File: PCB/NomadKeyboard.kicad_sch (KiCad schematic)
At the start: 94 parts, among them J1 4PIN, J2 OLED, P1 i2c_pin, P2 i2c_pin, SW1 SW_PUSH_LED, SW10 SW_PUSH_LED, SW11 SW_PUSH_LED, SW12 SW_PUSH_LED, SW13 SW_PUSH_LED, SW14 SW_PUSH_LED, SW15 SW_PUSH_LED, SW16 SW_PUSH_LED, SW17 SW_PUSH_LED, SW18 SW_PUSH_LED, SW19 SW_PUSH_LED, SW2 SW_PUSH_LED, SW20 SW_PUSH_LED, SW21 SW_PUSH_LED, SW22 SW_PUSH_LED, SW23 SW_PUSH_LED, SW24 SW_PUSH_LED, SW25 SW_PUSH_LED, SW26 SW_PUSH_LED, SW27 SW_PUSH_LED, SW28 SW_PUSH_LED, SW29 SW_PUSH_LED, SW3 SW_PUSH_LED, SW30 SW_PUSH_LED, SW31 SW_PUSH_LED, SW32 SW_PUSH_LED, SW33 SW_PUSH_LED, SW34 SW_PUSH_LED, SW4 SW_PUSH_LED, SW5 SW_PUSH_LED, SW6 SW_PUSH_LED, SW7 SW_PUSH_LED, SW8 SW_PUSH_LED, SW9 SW_PUSH_LED, U1 ProMicro

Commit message: Plated Mounting holes, STL File for top case, new Photos
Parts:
- TH5, TH6, TH7, TH8: footprint MountingHole:MountingHole_2.2mm_M2 -> SofleChoc:M2_HOLE_PCB
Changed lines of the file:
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@@
 			)
 		)
-		(property "Footprint" "MountingHole:MountingHole_2.2mm_M2"
+		(property "Footprint" "SofleChoc:M2_HOLE_PCB"
 			(at 38.1 179.07 0)
 			(effects
@@
 			)
 		)
-		(property "Footprint" "MountingHole:MountingHole_2.2mm_M2"
+		(property "Footprint" "SofleChoc:M2_HOLE_PCB"
 			(at 29.21 179.07 0)
 			(effects
@@
 			)
 		)
-		(property "Footprint" "MountingHole:MountingHole_2.2mm_M2"
+		(property "Footprint" "SofleChoc:M2_HOLE_PCB"
 			(at 46.99 179.07 0)
 			(effects
@@
 			)
 		)
-		(property "Footprint" "MountingHole:MountingHole_2.2mm_M2"
+		(property "Footprint" "SofleChoc:M2_HOLE_PCB"
 			(at 20.32 179.07 0)
 			(effects

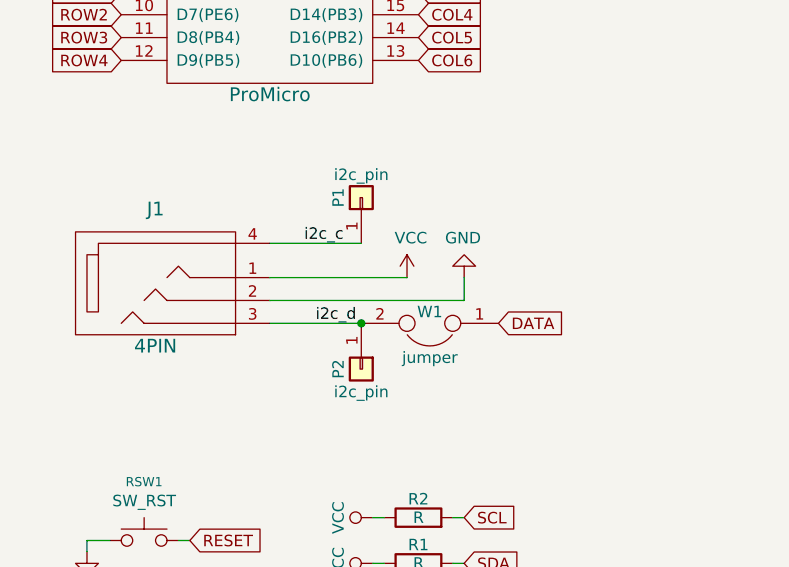
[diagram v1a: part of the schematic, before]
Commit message: Added a new MX variant of the PCB, moved mounting holes for the display cover so the spacers don't interfere with the display
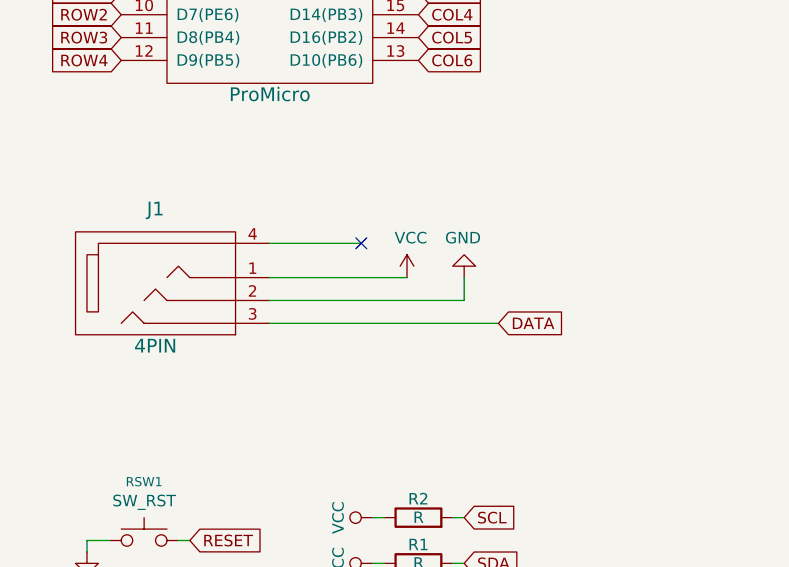
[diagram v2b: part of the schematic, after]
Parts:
- removed P1, P2: i2c_pin, SofleChoc:1pin_conn, symbol SofleKeyboard-rescue:i2c_pin-Lily58-cache-Lily58_Pro-rescue
- removed W1: jumper, Jumper:SolderJumper-2_P1.3mm_Open_Pad1.0x1.5mm, symbol SofleKeyboard-rescue:Jumper-Device
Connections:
- net i2c_d is gone; now on net DATA: J1.3
- net i2c_c: no longer names the net of J1.4
- no-connect marks 4 -> 5
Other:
- title: (none) -> Nomad Keyboard
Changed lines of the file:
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@@
 	(generator_version "8.0")
 	(paper "A4")
+	(title_block
+		(title "Nomad Keyboard")
+		(date "2024-11-08")
+		(rev "1.1")
+	)
 	(junction
 		(at 212.09 137.16)
@@
 	)
 	(junction
-		(at 54.61 78.74)
-		(diameter 0)
-		(color 0 0 0 0)
-	)
-	(junction
 		(at 232.41 137.16)
 		(diameter 0)
@@
 	)
 	(no_connect
+		(at 54.61 69.85)
+	)
+	(no_connect
 		(at 60.96 31.75)
 	)
@@
 	(wire
 		(pts
-			(xy 44.45 78.74) (xy 54.61 78.74)
+			(xy 44.45 78.74) (xy 69.85 78.74)
 		)
 		(stroke
@@
 		)
 	)
-	(label "i2c_d"
-		(at 49.53 78.74 0)
-		(fields_autoplaced yes)
-		(effects
-			(font
-				(size 1.27 1.27)
-			)
-			(justify left bottom)
-		)
-	)
-	(label "i2c_c"
-		(at 48.26 69.85 0)
-		(fields_autoplaced yes)
-		(effects
-			(font
-				(size 1.27 1.27)
-			)
-			(justify left bottom)
-		)
-	)
 	(global_label "ROW0"
 		(shape input)
@@
 					(unit 1)
 				)
-			)
-		)
-	)
-	(symbol
-		(lib_id "SofleKeyboard-rescue:i2c_pin-Lily58-cache-Lily58_Pro-rescue")
-		(at 54.61 64.77 90)
-		(unit 1)
-		(exclude_from_sim no)
-		(in_bom yes)
-		(on_board yes)
-		(dnp no)
-		(property "Reference" "P1"
-			(at 52.07 64.77 0)
-			(effects
-				(font
-					(size 1.27 1.27)
-				)
-			)
-		)
-		(property "Value" "i2c_pin"
-			(at 54.61 62.23 90)
-			(effects
-				(font
-					(size 1.27 1.27)
-				)
-			)
-		)
-		(property "Footprint" "SofleChoc:1pin_conn"
-			(at 54.61 64.77 0)
-			(effects
-				(font
-					(size 1.27 1.27)
-				)
-				(hide yes)
-			)
-		)
-		(property "Datasheet" ""
-			(at 54.61 64.77 0)
-			(effects
-				(font
-					(size 1.27 1.27)
-				)
-				(hide yes)
-			)
-		)
-		(property "Description" ""
-			(at 54.61 64.77 0)
-			(effects
-				(font
-					(size 1.27 1.27)
-				)
-				(hide yes)
-			)
-		)
-		(pin "1"
-		)
-		(instances
-			(project "NomadKeyboard"
-				(path "/eaee3b4b-85c3-461f-869e-93e0a5fc0df7"
-					(reference "P1")
-					(unit 1)
-				)
-			)
-		)
-	)
-	(symbol
-		(lib_id "SofleKeyboard-rescue:i2c_pin-Lily58-cache-Lily58_Pro-rescue")
-		(at 54.61 83.82 270)
-		(unit 1)
-		(exclude_from_sim no)
-		(in_bom yes)
-		(on_board yes)
-		(dnp no)
-		(property "Reference" "P2"
-			(at 52.07 83.82 0)
-			(effects
-				(font
-					(size 1.27 1.27)
-				)
-			)
-		)
-		(property "Value" "i2c_pin"
-			(at 54.61 86.36 90)
-			(effects
-				(font
-					(size 1.27 1.27)
-				)
-			)
-		)
-		(property "Footprint" "SofleChoc:1pin_conn"
-			(at 54.61 83.82 0)
-			(effects
-				(font
-					(size 1.27 1.27)
-				)
-				(hide yes)
-			)
-		)
-		(property "Datasheet" ""
-			(at 54.61 83.82 0)
-			(effects
-				(font
-					(size 1.27 1.27)
-				)
-				(hide yes)
-			)
-		)
-		(property "Description" ""
-			(at 54.61 83.82 0)
-			(effects
-				(font
-					(size 1.27 1.27)
-				)
-				(hide yes)
-			)
-		)
-		(pin "1"
-		)
-		(instances
-			(project "NomadKeyboard"
-				(path "/eaee3b4b-85c3-461f-869e-93e0a5fc0df7"
-					(reference "P2")
-					(unit 1)
-				)
-			)
-		)
-	)
-	(symbol
-		(lib_id "SofleKeyboard-rescue:Jumper-Device")
-		(at 62.23 78.74 180)
-		(unit 1)
-		(exclude_from_sim no)
-		(in_bom yes)
-		(on_board yes)
-		(dnp no)
-		(property "Reference" "W1"
-			(at 62.23 77.47 0)
-			(effects
-				(font
-					(size 1.27 1.27)
-				)
-			)
-		)
-		(property "Value" "jumper"
-			(at 62.23 82.55 0)
-			(effects
-				(font
-					(size 1.27 1.27)
-				)
-			)
-		)
-		(property "Footprint" "Jumper:SolderJumper-2_P1.3mm_Open_Pad1.0x1.5mm"
-			(at 62.23 78.74 0)
-			(effects
-				(font
-					(size 1.27 1.27)
-				)
-				(hide yes)
-			)
-		)
-		(property "Datasheet" ""
-			(at 62.23 78.74 0)
-			(effects
-				(font
-					(size 1.27 1.27)
-				)
-			)
-		)
-		(property "Description" ""
-			(at 62.23 78.74 0)
-			(effects
-				(font
-					(size 1.27 1.27)
-				)
-				(hide yes)
-			)
-		)
-		(pin "1"
-		)
-		(pin "2"
-		)
-		(instances
-			(project "NomadKeyboard"
-				(path "/eaee3b4b-85c3-461f-869e-93e0a5fc0df7"
-					(reference "W1")
-					(unit 1)
-				)
